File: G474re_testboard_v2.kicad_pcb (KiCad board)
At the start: 2 copper layers, 82 x 82 mm, 76 parts, among them J1 Conn_ST_STDC14, J10 Conn_01x02_Pin, J14 Conn_01x04_Socket, J15 Conn_01x04_Socket, J16 Conn_01x04_Socket, J17 Conn_01x04_Socket, J18 Conn_01x02_Socket, J19 Conn_01x02_Socket, J2 USB_C_Receptacle_USB2.0_16P, J20 Conn_01x02_Socket, J21 Conn_01x02_Socket, J22 Conn_01x02_Socket, J23 Conn_01x04_Socket, J26 Conn_01x02_Socket, J27 Conn_01x02_Socket, J28 Conn_01x02_Socket, J3 Conn_01x02_Socket, J30 Conn_01x04_Pin, J4 Conn_01x02_Socket, J5 Conn_01x04_Socket, J6 Conn_01x08_Socket, J7 Conn_01x04_Socket, J8 Conn_01x04_Socket, J9 Conn_01x04_Socket, SW1 SW_Push, SW2 SW_Push, SW3 SW_Push, SW4 SW_SPDT, U1 STM32G474RETx, U2 AMS1117-5.0, U3 AMS1117-3.3, U4 ATA6561, U5 ATA6561, Y1 TSX-3225 24.0000MF20G-AC3

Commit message: 修正テスト
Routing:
- net GND: vias 266 -> 267

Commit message: kicad10.0.3test
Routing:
- net GND: vias 267 -> 266
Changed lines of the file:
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@@
-	)
-	(via
-		(at 116 100.31)
-		(size 0.6)
-		(drill 0.3)
-		(layers "F.Cu" "B.Cu")
-		(free yes)
-		(net "GND")
 	)
 	(via

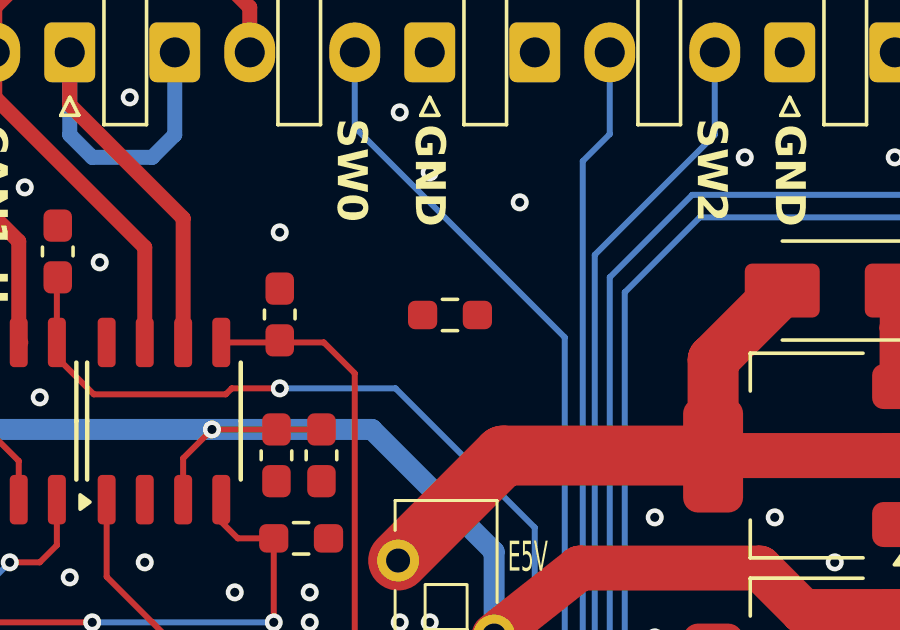
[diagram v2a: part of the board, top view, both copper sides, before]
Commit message: 余計な抵抗を削除
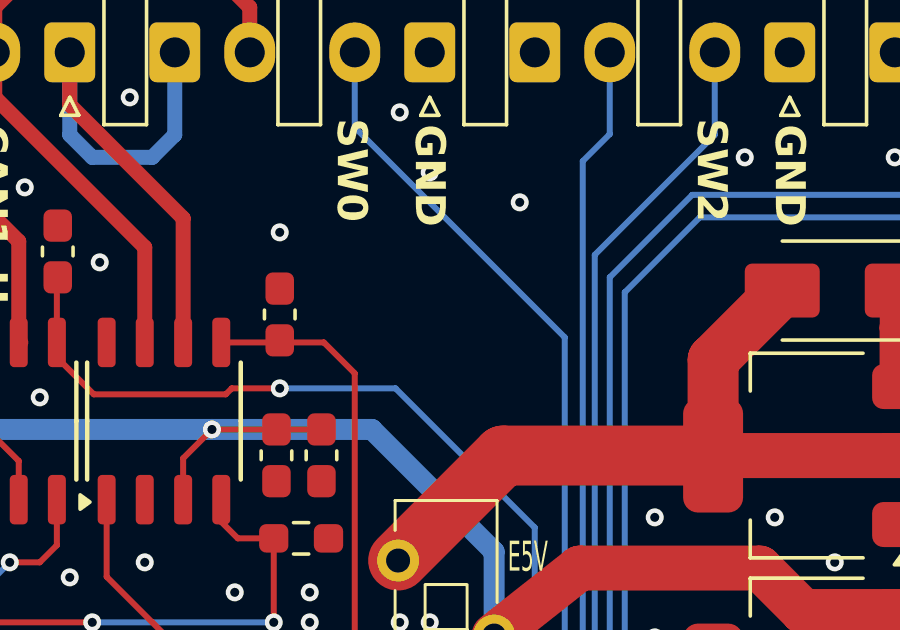
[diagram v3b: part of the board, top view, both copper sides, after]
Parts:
- removed R8: 10k, Resistor_SMD:R_0603_1608Metric_Pad0.98x0.95mm_HandSolder
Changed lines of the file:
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@@
-		)
-	)
-	(footprint "Resistor_SMD:R_0603_1608Metric_Pad0.98x0.95mm_HandSolder"
-		(layer "F.Cu")
-		(at 88.675 79.565)
-		(descr "Resistor SMD 0603 (1608 Metric), square (rectangular) end terminal, IPC-7351 nominal with elongated pad for handsoldering. (Body size source: IPC-SM-782 page 72, https://www.pcb-3d.com/wordpress/wp-content/uploads/ipc-sm-782a_amendment_1_and_2.pdf)")
-		(tags "resistor handsolder")
-		(property "Reference" "R8"
-			(at 0 -1.43 0)
-			(layer "F.SilkS")
-			(hide yes)
-			(effects
-				(font
-					(size 1 1)
-					(thickness 0.15)
-				)
-			)
-		)
-		(property "Value" "10k"
-			(at 0 1.43 0)
-			(layer "F.Fab")
-			(effects
-				(font
-					(size 1 1)
-					(thickness 0.15)
-				)
-			)
-		)
-		(property "Datasheet" ""
-			(at 0 0 0)
-			(layer "F.Fab")
-			(hide yes)
-			(effects
-				(font
-					(size 1.27 1.27)
-				)
-			)
-		)
-		(property "Description" "Resistor"
-			(at 0 0 0)
-			(layer "F.Fab")
-			(hide yes)
-			(effects
-				(font
-					(size 1.27 1.27)
-				)
-			)
-		)
-		(property "KiLib_Generator" "SMD_2terminal_chip_molded"
-			(at 0 0 0)
-			(layer "F.SilkS")
-			(hide yes)
-			(effects
-				(font
-					(size 1 1)
-					(thickness 0.15)
-				)
-			)
-		)
-		(property "KLC_S3.3" ""
-			(at 0 0 0)
-			(unlocked yes)
-			(layer "F.Fab")
-			(hide yes)
-			(effects
-				(font
-					(size 1 1)
-					(thickness 0.15)
-				)
-			)
-		)
-		(property "KLC_S4.1" ""
-			(at 0 0 0)
-			(unlocked yes)
-			(layer "F.Fab")
-			(hide yes)
-			(effects
-				(font
-					(size 1 1)
-					(thickness 0.15)
-				)
-			)
-		)
-		(property "LCSC" " C25804"
-			(at 0 0 0)
-			(unlocked yes)
-			(layer "F.Fab")
-			(hide yes)
-			(effects
-				(font
-					(size 1 1)
-					(thickness 0.15)
-				)
-			)
-		)
-		(property ki_fp_filters "R_*")
-		(sheetname "/G474/")
-		(sheetfile "G474.kicad_sch")
-		(units
-			(unit
-				(name "A")
-				(pins "1" "2")
-			)
-		)
-		(attr smd)
-		(duplicate_pad_numbers_are_jumpers no)
-		(fp_line
-			(start -0.254724 -0.5225)
-			(end 0.254724 -0.5225)
-			(stroke
-				(width 0.12)
-				(type solid)
-			)
-			(layer "F.SilkS")
-		)
-		(fp_line
-			(start -0.254724 0.5225)
-			(end 0.254724 0.5225)
-			(stroke
-				(width 0.12)
-				(type solid)
-			)
-			(layer "F.SilkS")
-		)
-		(fp_rect
-			(start -1.65 -0.73)
-			(end 1.65 0.73)
-			(stroke
-				(width 0.05)
-				(type solid)
-			)
-			(fill no)
-			(layer "F.CrtYd")
-		)
-		(fp_rect
-			(start -0.8 -0.4125)
-			(end 0.8 0.4125)
-			(stroke
-				(width 0.1)
-				(type solid)
-			)
-			(fill no)
-			(layer "F.Fab")
-		)
-		(fp_text user "${REFERENCE}"
-			(at 0 0 0)
-			(layer "F.Fab")
-			(effects
-				(font
-					(size 0.4 0.4)
-					(thickness 0.06)
-				)
-			)
-		)
-		(pad "1" smd roundrect
-			(at -0.9125 0)
-			(size 0.975 0.95)
-			(layers "F.Cu" "F.Mask" "F.Paste")
-			(roundrect_rratio 0.25)
-			(net "/G474/CAN1_ON")
-			(pintype "passive")
-		)
-		(pad "2" smd roundrect
-			(at 0.9125 0)
-			(size 0.975 0.95)
-			(layers "F.Cu" "F.Mask" "F.Paste")
-			(roundrect_rratio 0.25)
-			(net "GND")
-			(pintype "passive")
-		)
-		(embedded_fonts no)
-		(model "${KICAD10_3DMODEL_DIR}/Resistor_SMD.3dshapes/R_0603_1608Metric.step"
-			(offset
-				(xyz 0 0 0)
-			)
-			(scale
-				(xyz 1 1 1)
-			)
-			(rotate
-				(xyz 0 0 0)
-			)
 		)
 	)
